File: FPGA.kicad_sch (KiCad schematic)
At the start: 112 parts, among them U11 IS62WV51216BLL-55TLI, U7 CAT24C128, U8 LFE5U-25F-8MG285C, U9 W25Q128JVP, X1 27MHz

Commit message: Continue routing
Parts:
- removed TP19, TP20, TP23, TP24: TestPoint, TestPoint:TestPoint_THTPad_D1.5mm_Drill0.7mm, symbol Connector:TestPoint
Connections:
- net scl: now also U8.A7 (PR8B)
- net sda: now also U8.B6 (PR8A)
- net at U8.B7 (PR2B/S0_IN): now also R70.1
- net at U8.C6 (PR5B): now also R68.1
- net at U8.C7 (PR2A): now also R69.1
- net at U8.D6 (PR5A): now also R67.1
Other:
- moved on the sheet: R67, R68, R69, R70

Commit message: continue routing
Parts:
- removed TP25, TP26, TP27, TP40, TP41, TP42, TP43, TP44, TP45, TP46, TP58, TP59, TP60, TP61, TP62, TP63, TP64: TestPoint, TestPoint:TestPoint_THTPad_D1.5mm_Drill0.7mm, symbol Connector:TestPoint

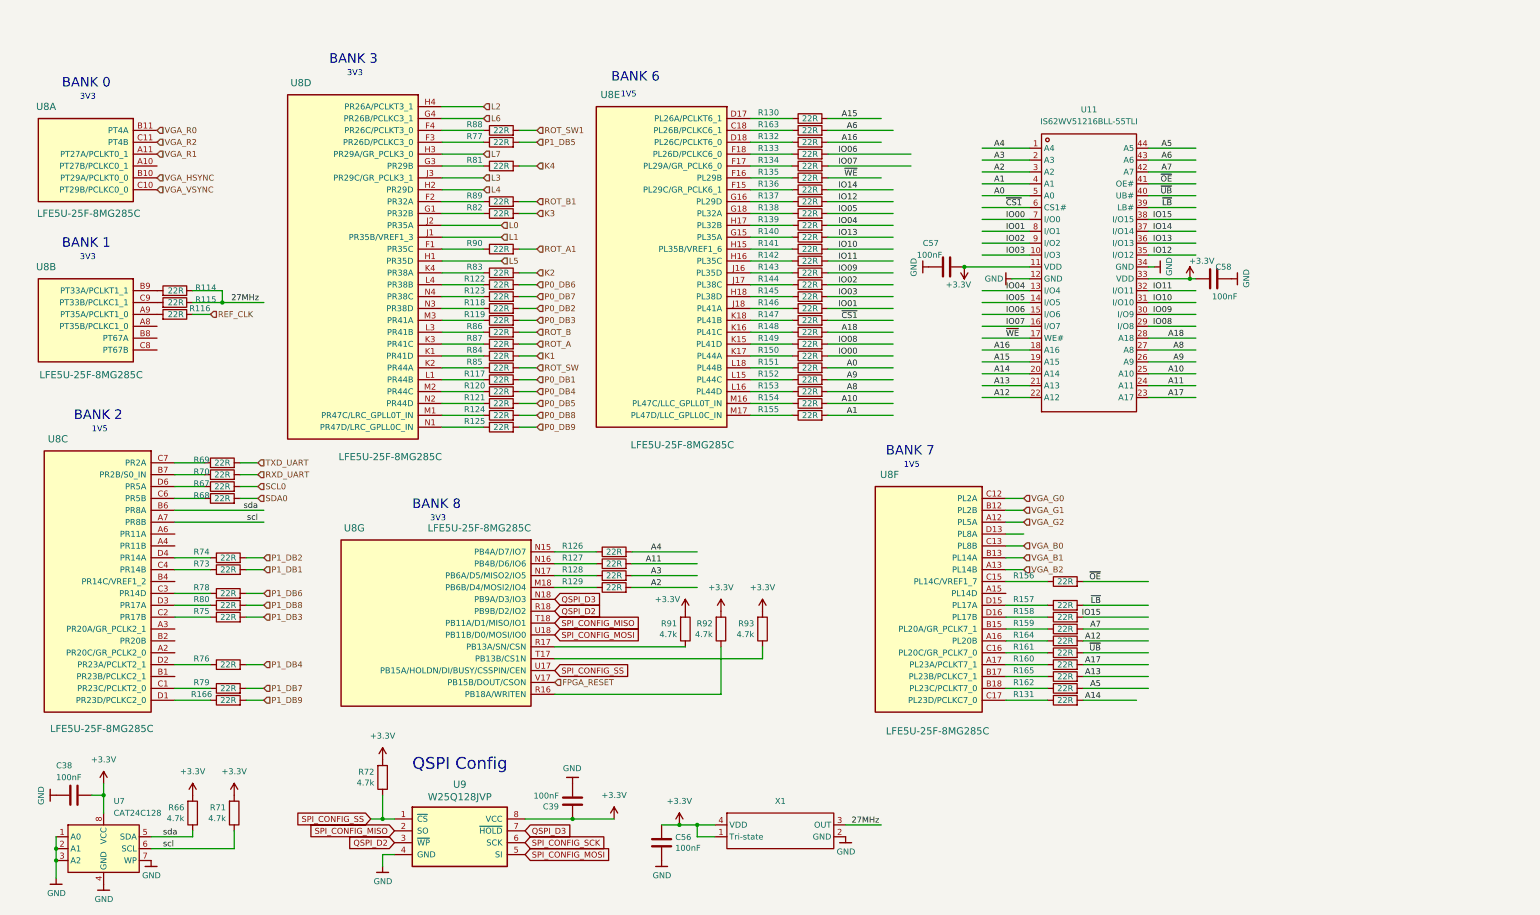
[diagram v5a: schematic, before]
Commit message: Fix dcr for schematics
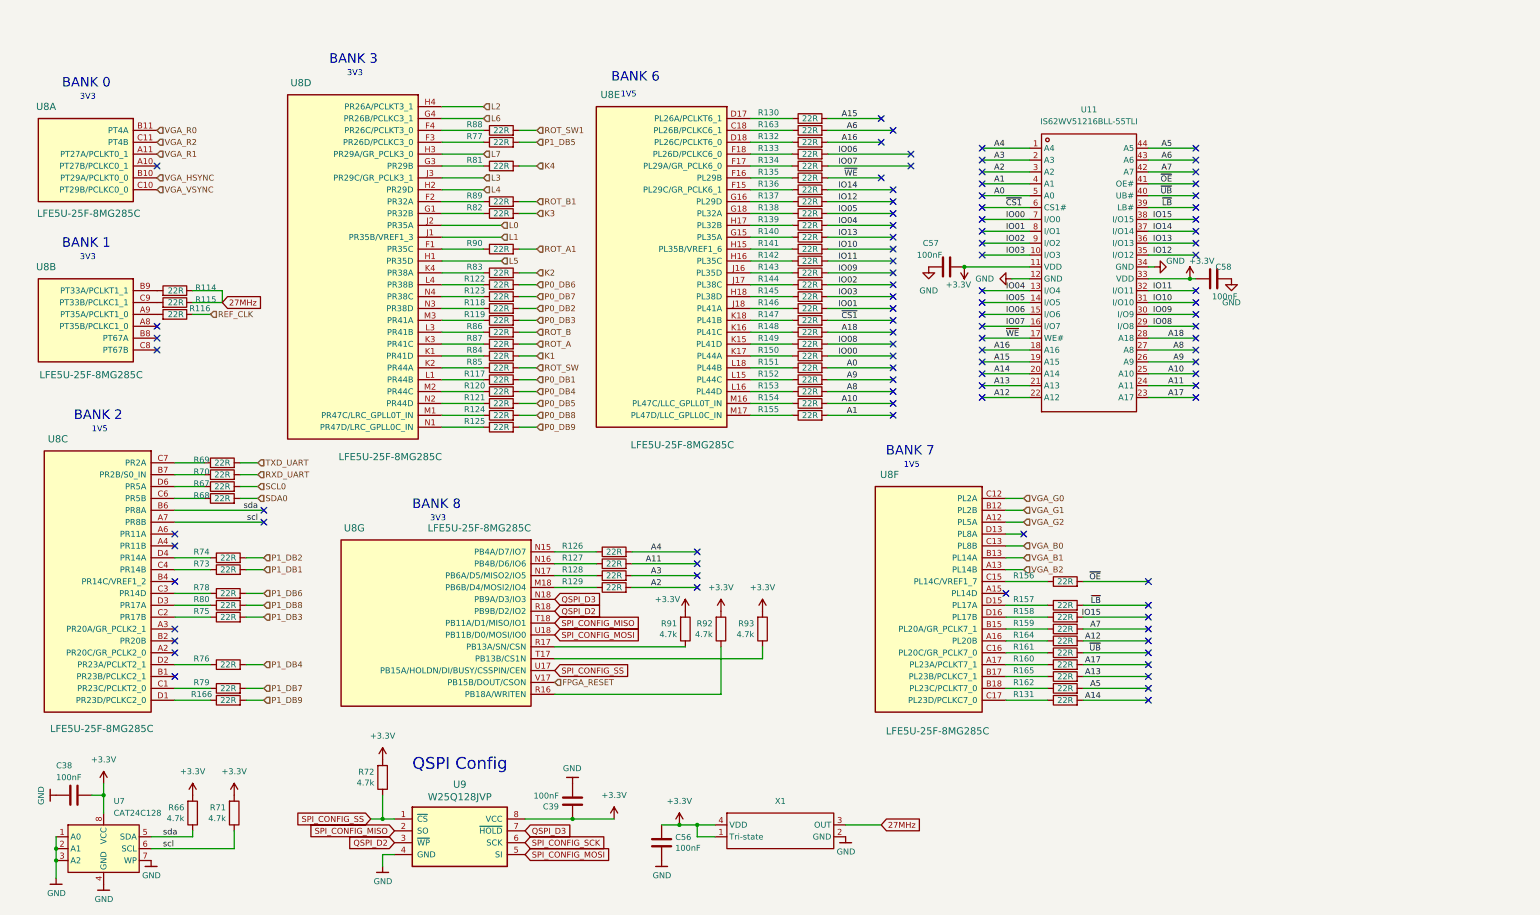
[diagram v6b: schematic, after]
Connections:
- no-connect marks 0 -> 95
